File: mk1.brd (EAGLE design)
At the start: 31.2 x 31.6 mm, 18 parts, among them U1 ATMEGA328P-AU

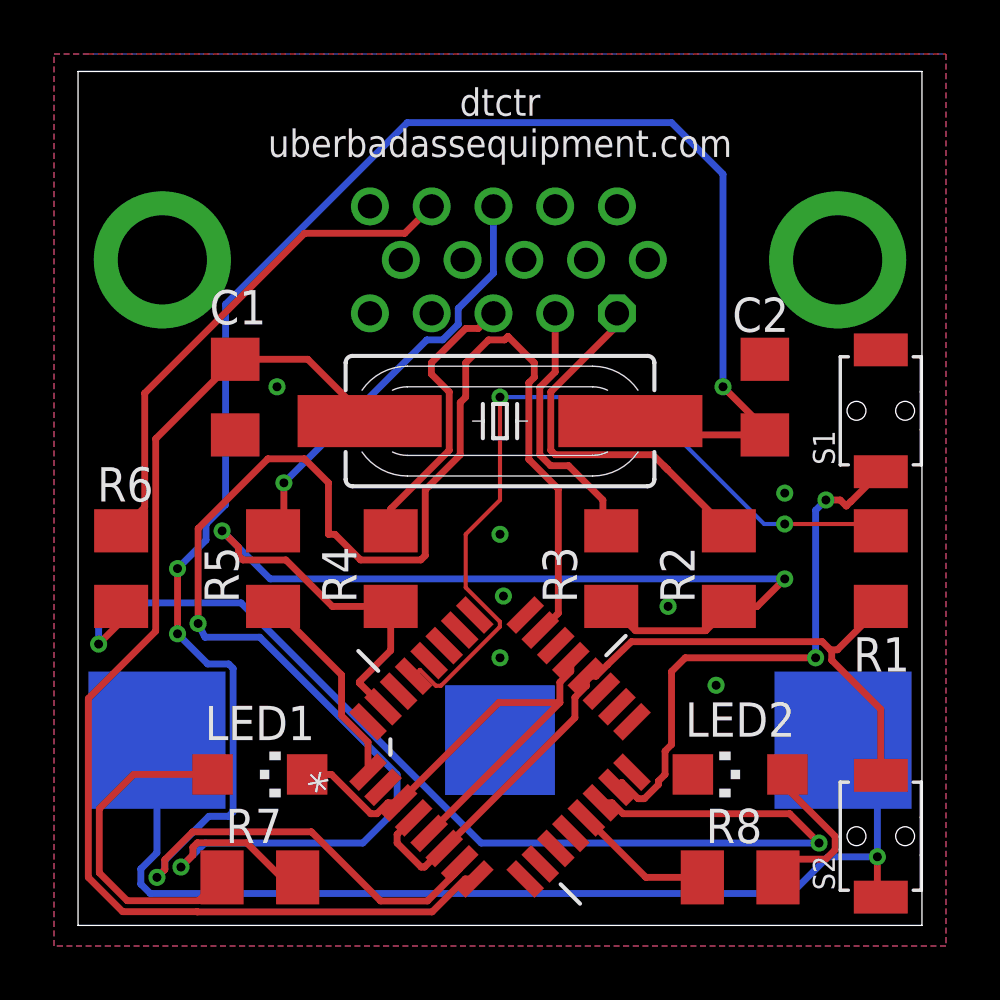
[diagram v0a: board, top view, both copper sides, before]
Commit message: Some cleanup. Moved battery holder, less risk of shorting the battery. Changed pins for LEDs for easier routing.
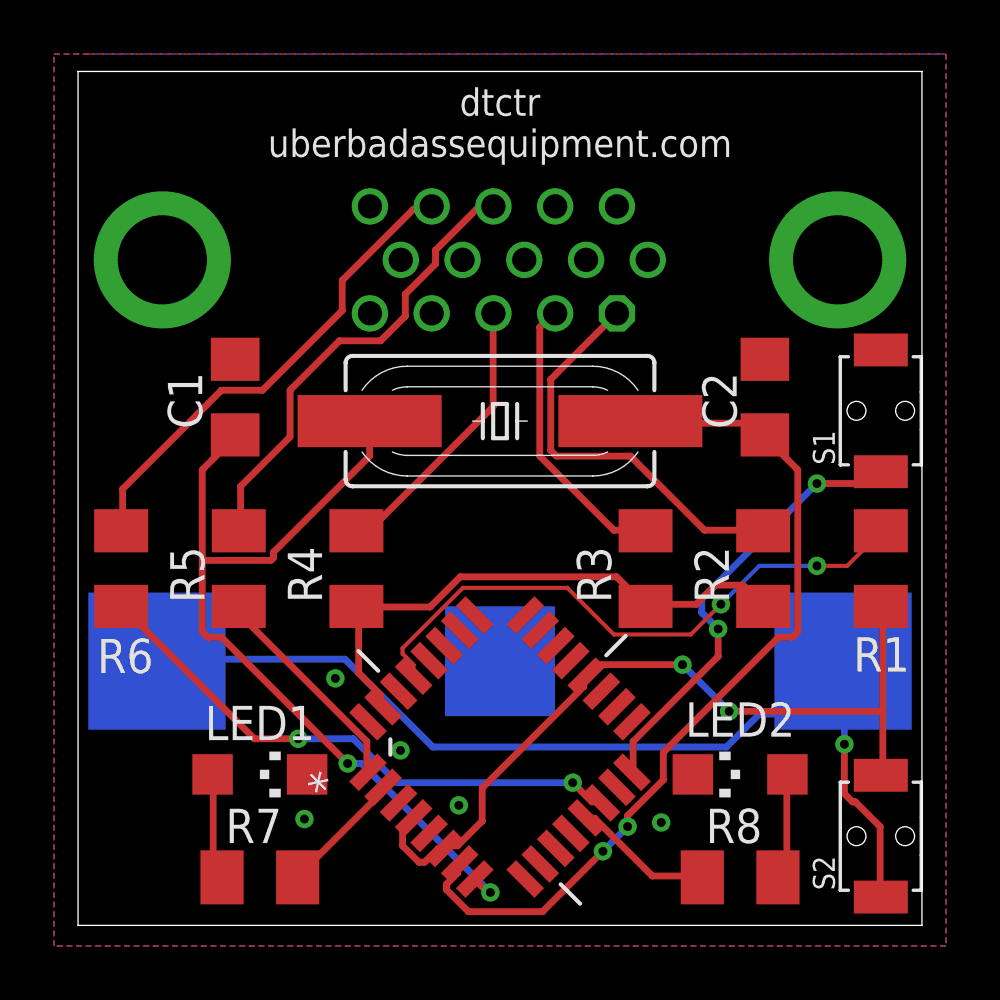
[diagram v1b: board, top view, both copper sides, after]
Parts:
- C1, C2: value (none) -> 22pF
- Q1: value (none) -> 16MHz
- R5, R6, R7, R8: value (none) -> 68R
- moved U$1 2.92 mm to (16.5, 11.8)
- moved R3 1.27 mm to (21.9, 15.2)
- moved R4 1.27 mm to (11.2, 15.2)
- moved R2 1.27 mm to (26.3, 15.2)
- moved R5 1.27 mm to (6.84, 15.2)
- turned C1 to 90 degrees
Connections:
- removed net N$14: U1.26
- removed net N$5: R7.2, U1.23
- new net N$1: R7.2, U1.2
- net N$15: now also U1.16; no longer U1.15
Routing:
- net N$5: track 62.9 -> 0.00 mm, vias 2 -> 0
- net XTAL2: track 76.2 -> 32.7 mm, vias 4 -> 2
- net VSYNC: track 42.6 -> 20.8 mm
- net N$4: track 41.9 -> 20.8 mm, vias 2 -> 0
- net GND: track 20.2 -> 0.00 mm, vias 7 -> 5
- net XTAL1: track 42.7 -> 32.5 mm, vias 0 -> 2
- net N$6: track 12.9 -> 3.96 mm
- net RESET: track 30.1 -> 22.2 mm
- net N$1: track 0.00 -> 4.67 mm
- net N$15: track 20.7 -> 16.6 mm
- net N$7: track 6.06 -> 3.96 mm
- net N$12: track 15.7 -> 17.2 mm, vias 1 -> 0
- net PWR: track 39.9 -> 38.6 mm
- net N$8: track 14.2 -> 15.2 mm
- net N$11: track 18.9 -> 18.0 mm
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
